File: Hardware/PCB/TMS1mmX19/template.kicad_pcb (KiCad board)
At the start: 20 copper layers, 152.4 x 152.4 mm, 0 parts

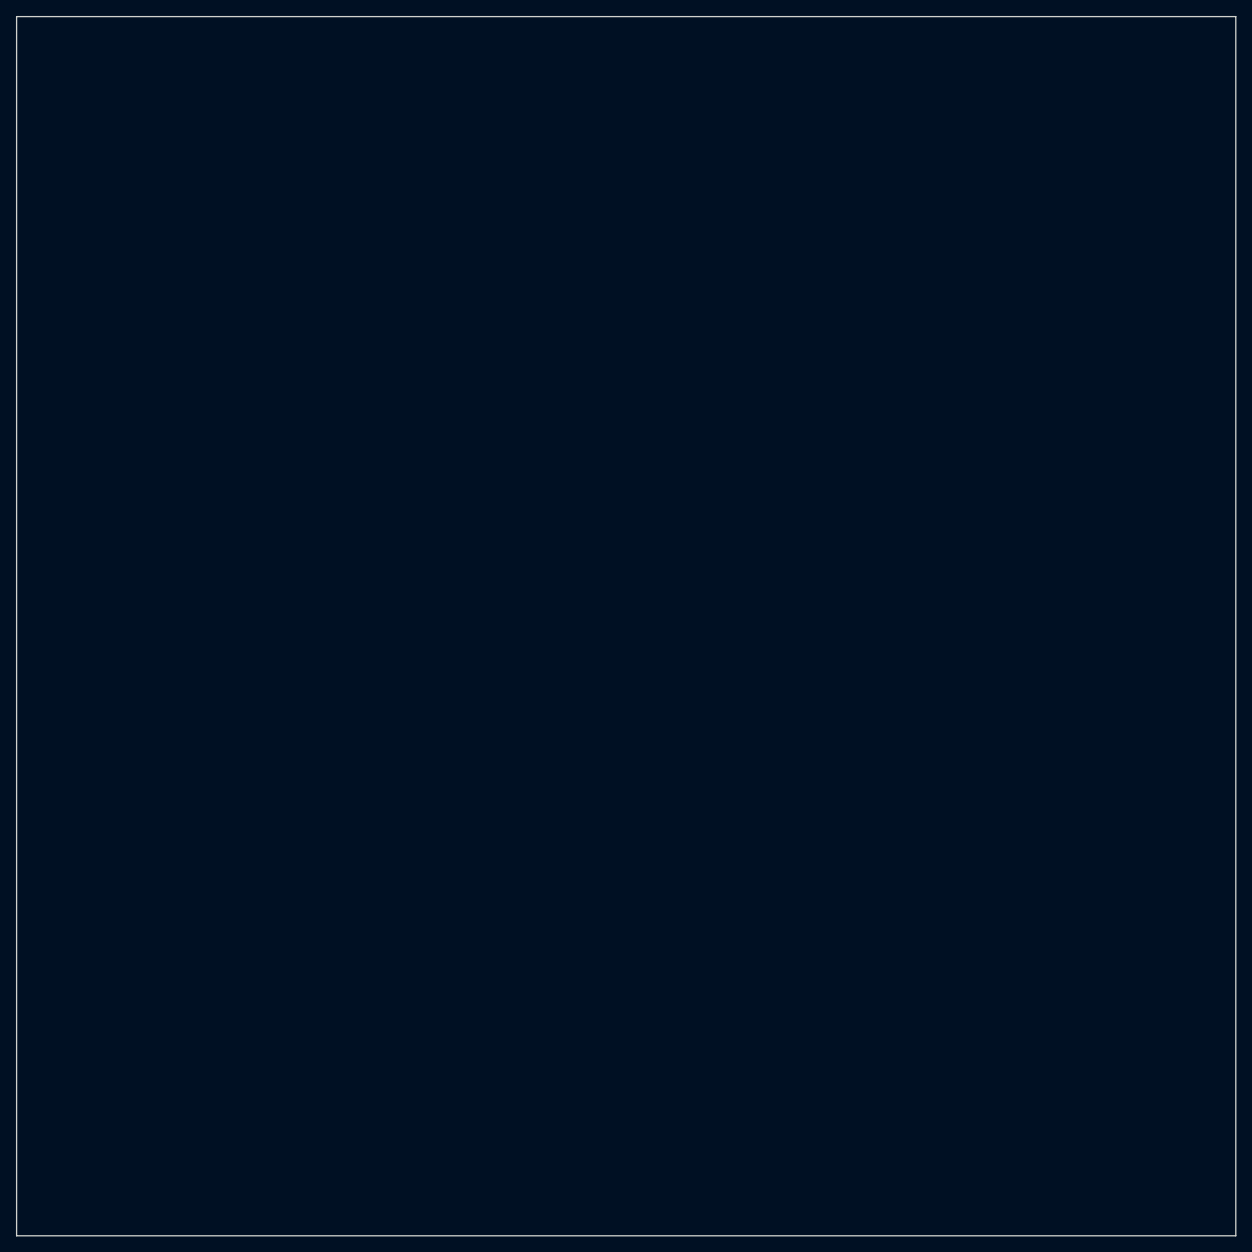
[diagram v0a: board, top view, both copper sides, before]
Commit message: First production-ready PCB/TMS1mmX19
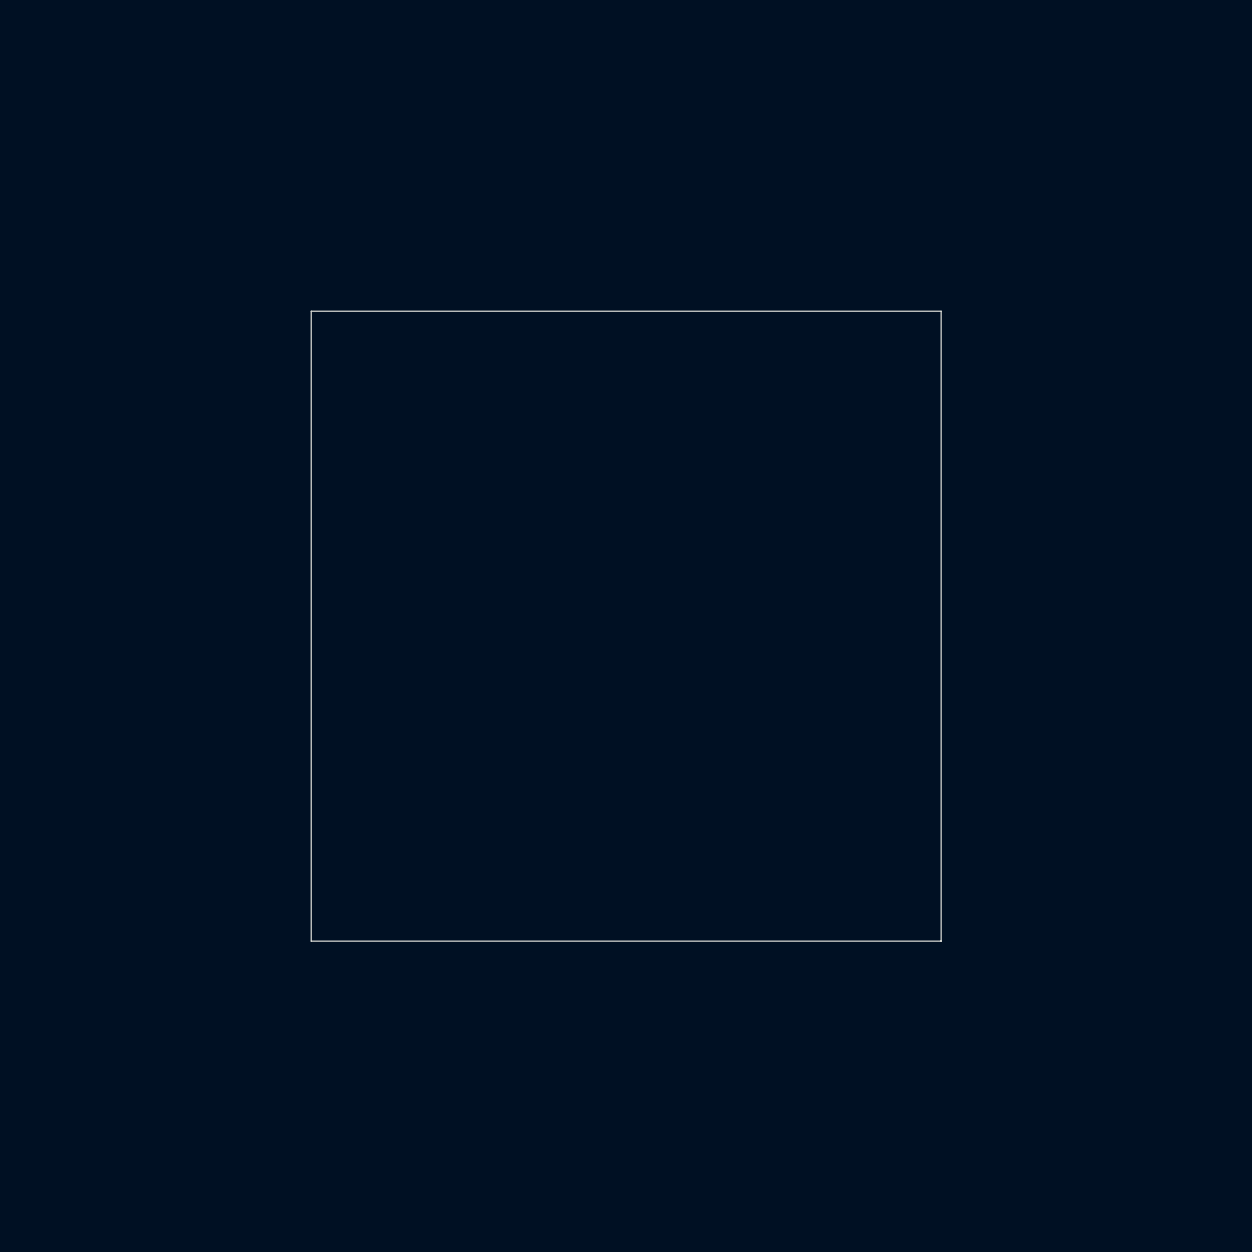
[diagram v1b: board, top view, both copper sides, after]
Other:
- board size 152.4 x 152.4 mm -> 78.7 x 78.7 mm
- copper layers 20 -> 16
- rule pad_to_mask_clearance: 0.2 -> 0.2032
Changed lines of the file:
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@@
-(kicad_pcb (version 20170123) (host pcbnew "(2017-05-18 revision 2a3a699)-master")
+(kicad_pcb (version 20170123) (host pcbnew "(2017-07-14 revision d3b382c28)-master")
   (general
-    (links 0)
-    (no_connects 0)
-    (area 63.424999 31.674999 215.975001 184.225001)
-    (thickness 3.175)
+    (thickness 1.92024)
     (drawings 4)
     (tracks 0)
@@
   (page USLetter)
   (title_block
-    (title "Topmetal-S sensor tiled plane, 10cm diameter version")
-    (date 2017-03-28)
+    (title "Topmetal-S sensor tiled plane, 19 sensors")
+    (date 2017-07-19)
     (rev 0)
     (company LBNL)
@@
     (2 In2.Cu signal)
     (3 In3.Cu signal)
-    (4 In4.Cu signal)
+    (4 In4.Cu power)
     (5 In5.Cu signal)
     (6 In6.Cu signal)
-    (7 In7.Cu signal)
-    (8 In8.Cu signal)
+    (7 In7.Cu power)
+    (8 In8.Cu power)
     (9 In9.Cu signal)
     (10 In10.Cu signal)
-    (11 In11.Cu signal)
+    (11 In11.Cu power)
     (12 In12.Cu signal)
     (13 In13.Cu signal)
-    (14 In14.Cu signal)
-    (15 In15.Cu signal)
-    (16 In16.Cu signal)
-    (17 In17.Cu signal)
-    (18 In18.Cu signal)
+    (14 In14.Cu power)
     (31 B.Cu signal)
     (32 B.Adhes user)
@@
     (user_trace_width 0.1524)
     (user_trace_width 0.2032)
+    (user_trace_width 0.254)
+    (user_trace_width 0.3048)
+    (user_trace_width 0.4064)
+    (user_trace_width 0.508)
+    (user_trace_width 0.6096)
     (trace_clearance 0.1016)
     (zone_clearance 0.508)
@@
     (user_via 0.5588 0.2032)
     (user_via 0.7112 0.3556)
+    (user_via 0.8636 0.508)
+    (user_via 1.016 0.508)
+    (user_via 1.27 0.635)
     (uvia_size 0.3048)
     (uvia_drill 0.1016)
@@
     (pad_size 1.2 0.9)
     (pad_drill 0)
-    (pad_to_mask_clearance 0.2)
+    (pad_to_mask_clearance 0.2032)
     (aux_axis_origin 0 0)
     (visible_elements FFFFFF7F)
@@
     (uvia_dia 0.3048)
     (uvia_drill 0.1016)
-    (diff_pair_gap 0.2032)
+    (diff_pair_gap 0.1778)
     (diff_pair_width 0.1016)
   )
-  (gr_line (start 63.5 31.75) (end 215.9 31.75) (layer Edge.Cuts) (width 0.15))
-  (gr_line (start 215.9 31.75) (end 215.9 184.15) (layer Edge.Cuts) (width 0.15))
-  (gr_line (start 63.5 184.15) (end 215.9 184.15) (layer Edge.Cuts) (width 0.15))
-  (gr_line (start 63.5 31.75) (end 63.5 184.15) (layer Edge.Cuts) (width 0.15))
+  (gr_line (start 100.33 68.58) (end 179.07 68.58) (layer Edge.Cuts) (width 0.15))
+  (gr_line (start 179.07 68.58) (end 179.07 147.32) (layer Edge.Cuts) (width 0.15))
+  (gr_line (start 100.33 147.32) (end 179.07 147.32) (layer Edge.Cuts) (width 0.15))
+  (gr_line (start 100.33 68.58) (end 100.33 147.32) (layer Edge.Cuts) (width 0.15))
 )
